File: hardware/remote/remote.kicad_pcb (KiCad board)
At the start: 2 copper layers, 106.7 x 86.4 mm, 27 parts

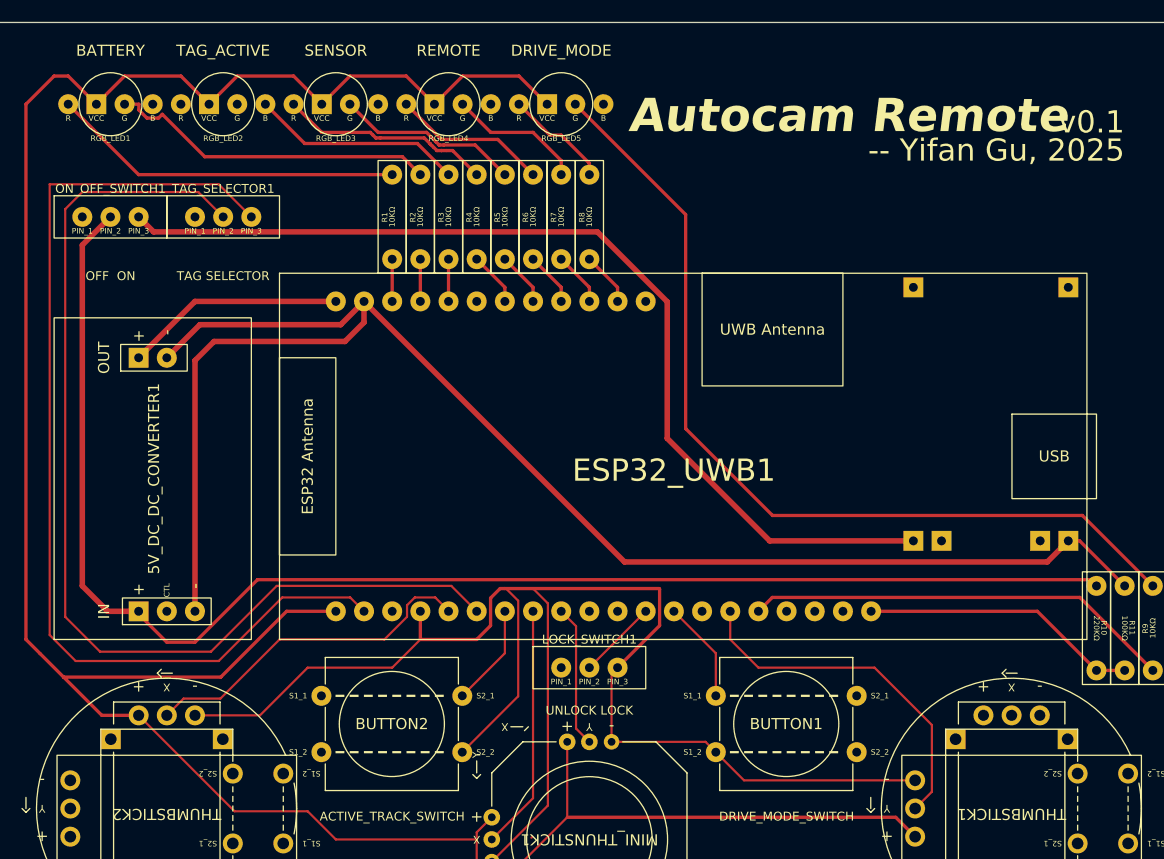
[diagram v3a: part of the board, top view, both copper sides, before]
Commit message: remote: Add UWB selector switch.
This switch will choose whether to use tag or the remote for the
distance measurement.

Also updated the PIN number and moved all non-uwb task to a separate
core.
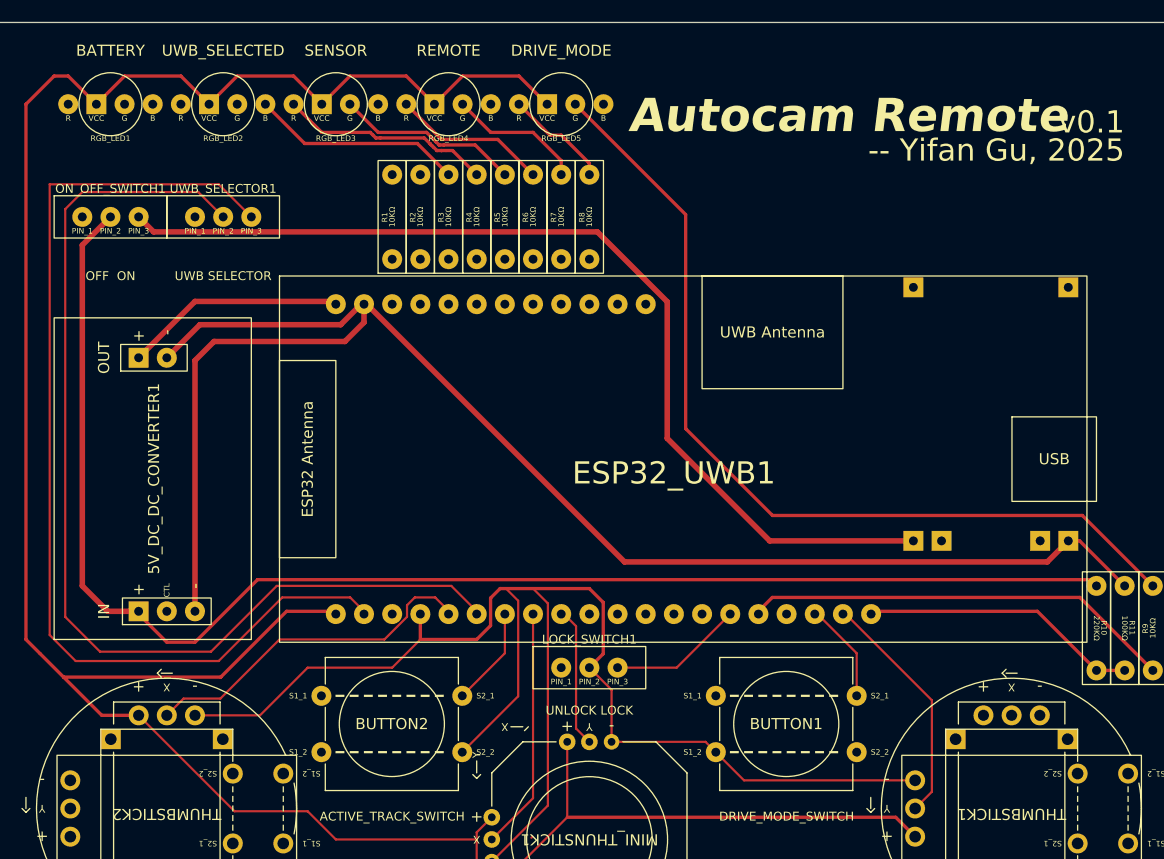
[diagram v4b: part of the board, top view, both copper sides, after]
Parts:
- RGB_LED2: value TAG_ACTIVE -> UWB_SELECTED
- UWB_SELECTOR1: renamed from TAG_SELECTOR1; value TAG SELECTOR -> UWB SELECTOR
- moved ESP32_UWB1 0.25 mm to (119.4, 83.8)
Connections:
- BUTTON1 pad 1: Net-(BUTTON1-S1_1) -> unconnected-(BUTTON1-S1_1-Pad1)
- BUTTON1 pad 3: unconnected-(BUTTON1-S2_1-Pad3) -> Net-(BUTTON1-S2_1)
- ESP32_UWB1 pad 12: Net-(ESP32_UWB1-IO25) -> unconnected-(ESP32_UWB1-IO25-Pad12)
- ESP32_UWB1 pad 13: Net-(BUTTON1-S1_1) -> unconnected-(ESP32_UWB1-IO26-Pad13)
- ESP32_UWB1 pad 18: unconnected-(ESP32_UWB1-IO35-Pad18) -> Net-(BUTTON1-S2_1)
- ESP32_UWB1 pad 19: unconnected-(ESP32_UWB1-IO36-Pad19) -> Net-(ESP32_UWB1-IO36)
- LOCK_SWITCH1 pad 2: Net-(ESP32_UWB1-IO25) -> Net-(BUTTON1-S1_2)
- LOCK_SWITCH1 pad 3: Net-(BUTTON1-S1_2) -> Net-(ESP32_UWB1-IO32)
- THUMBSTICK1 pad 5: Net-(ESP32_UWB1-IO32) -> Net-(ESP32_UWB1-IO36)
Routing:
- net Net-(RGB_LED1-R): track 31.8 -> 0.00 mm
- net Net-(RGB_LED1-G): track 29.9 -> 0.00 mm
- net Net-(ESP32_UWB1-IO36): track 0.00 -> 21.7 mm
- net Net-(ESP32_UWB1-IO32): track 32.1 -> 12.9 mm
- net Net-(BUTTON1-S2_1): track 0.00 -> 9.19 mm
- net Net-(BUTTON1-S1_1): track 9.19 -> 0.00 mm
- net Net-(ESP32_UWB1-IO25): track 7.18 -> 0.00 mm
- net Net-(BUTTON1-S1_2): track 139.7 -> 132.9 mm
- net Net-(ESP32_UWB1-IO22): track 4.86 -> 0.00 mm
- net Net-(ESP32_UWB1-IO16): track 4.86 -> 0.00 mm
- net Net-(ESP32_UWB1-IO5): track 4.86 -> 0.00 mm
- net Net-(ESP32_UWB1-IO21): track 4.86 -> 0.00 mm
- net Net-(ESP32_UWB1-IO17): track 4.86 -> 0.00 mm
- net Net-(ESP32_UWB1-IO3): track 3.81 -> 0.00 mm
- net Net-(ESP32_UWB1-IO1): track 3.81 -> 0.00 mm
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
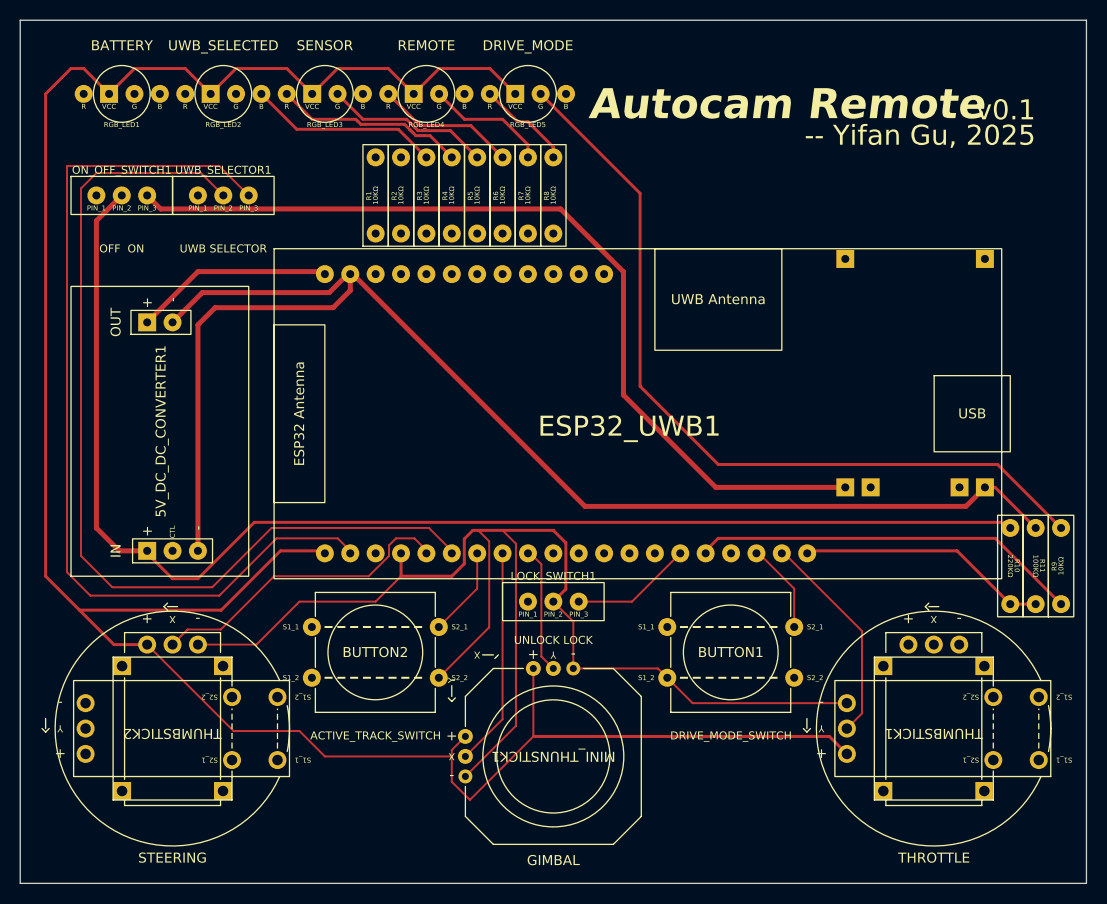
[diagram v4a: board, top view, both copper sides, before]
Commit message: hardware: Reroute the wires to fix unavailable PINs.
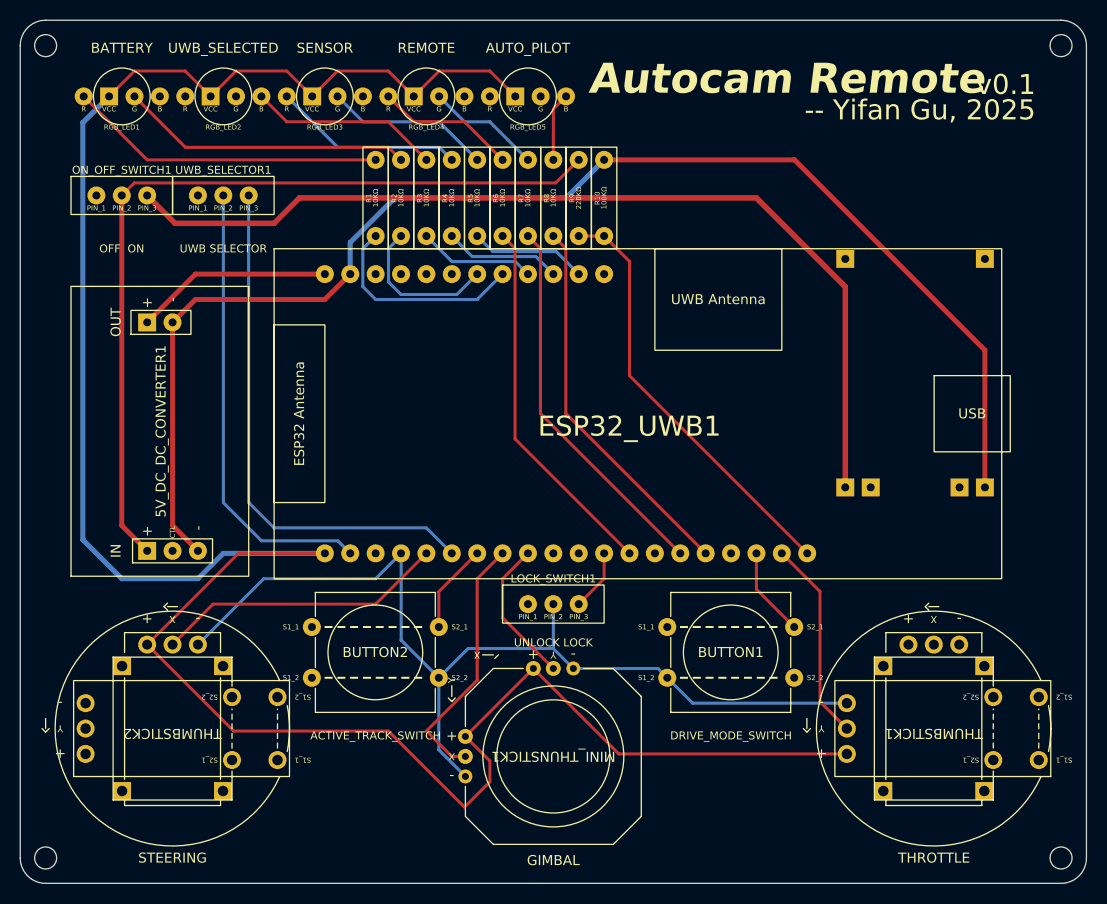
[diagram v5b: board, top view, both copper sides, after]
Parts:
- removed the R8 at (147.3, 82.3)
- added REF**: MountingHole_2.2mm_M2, MountingHole:MountingHole_2.2mm_M2, F.Cu at (198.1, 144.8)
- added REF**: MountingHole_2.2mm_M2, MountingHole:MountingHole_2.2mm_M2, F.Cu at (198.1, 63.5)
- added REF**: MountingHole_2.2mm_M2, MountingHole:MountingHole_2.2mm_M2, F.Cu at (96.5, 144.8)
- added REF**: MountingHole_2.2mm_M2, MountingHole:MountingHole_2.2mm_M2, F.Cu at (96.5, 63.5)
- RGB_LED5: value DRIVE_MODE -> AUTO_PILOT
- moved R8 62.7 mm to (147.3, 82.5)
- moved R10 52.1 mm to (152.4, 82.5), turned to 90 degrees
- moved R9 52.1 mm to (149.9, 82.5), turned to 90 degrees
- moved R6 2.55 mm to (142.2, 82.5)
- moved R7 2.55 mm to (144.8, 82.5)
- moved LOCK_SWITCH1 0.25 mm to (144.8, 119.4)
- moved R1 0.25 mm to (129.5, 82.5)
- moved R2 0.25 mm to (132.1, 82.5)
- moved R3 0.25 mm to (134.6, 82.5)
- moved R4 0.25 mm to (137.2, 82.5)
- moved R5 0.25 mm to (139.7, 82.5)
- moved RGB_LED1 0.25 mm to (104.1, 68.6)
- moved RGB_LED2 0.25 mm to (114.3, 68.6)
- moved RGB_LED3 0.25 mm to (124.5, 68.6)
- moved RGB_LED4 0.25 mm to (134.6, 68.6)
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- renumbered R11 to R10, R7 to R6, R6 to R7, R9 to R8, R10 to R9
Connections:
- ESP32_UWB1 pad 12: unconnected-(ESP32_UWB1-IO25-Pad12) -> Net-(ESP32_UWB1-IO25)
- ESP32_UWB1 pad 13: unconnected-(ESP32_UWB1-IO26-Pad13) -> Net-(ESP32_UWB1-IO26)
- ESP32_UWB1 pad 23: Net-(ESP32_UWB1-IO3) -> unconnected-(ESP32_UWB1-IO3-Pad23)
- ESP32_UWB1 pad 24: Net-(ESP32_UWB1-IO1) -> unconnected-(ESP32_UWB1-IO1-Pad24)
- ESP32_UWB1 pad 25: Net-(ESP32_UWB1-IO0) -> unconnected-(ESP32_UWB1-IO0-Pad25)
- LOCK_SWITCH1 pad 3: Net-(ESP32_UWB1-IO32) -> Net-(ESP32_UWB1-IO25)
- R1 pad 1: Net-(ESP32_UWB1-IO3) -> Net-(ESP32_UWB1-IO16)
- R10 pad 1: Net-(3.7V_BATTERY_CHARGER1-OUT-) -> Net-(ESP32_UWB1-IO39)
- R10 pad 2: Net-(ESP32_UWB1-IO39) -> Net-(3.7V_BATTERY_CHARGER1-OUT-)
- R2 pad 1: Net-(ESP32_UWB1-IO1) -> Net-(ESP32_UWB1-IO5)
- R3 pad 1: Net-(ESP32_UWB1-IO0) -> Net-(ESP32_UWB1-IO17)
- R4 pad 1: Net-(ESP32_UWB1-IO5) -> Net-(ESP32_UWB1-IO21)
- R5 pad 1: Net-(ESP32_UWB1-IO16) -> Net-(ESP32_UWB1-IO22)
- R6 pad 1: Net-(ESP32_UWB1-IO21) -> Net-(ESP32_UWB1-IO26)
- R6 pad 2: Net-(RGB_LED4-G) -> Net-(RGB_LED4-R)
- R7 pad 1: Net-(ESP32_UWB1-IO17) -> Net-(ESP32_UWB1-IO32)
- R7 pad 2: Net-(RGB_LED4-R) -> Net-(RGB_LED4-G)
- R8 pad 2: Net-(RGB_LED5-G) -> Net-(RGB_LED5-B)
- R9 pad 1: Net-(5V_DC_DC_CONVERTER1-IN_+) -> Net-(ESP32_UWB1-IO39)
- R9 pad 2: Net-(ESP32_UWB1-IO39) -> Net-(5V_DC_DC_CONVERTER1-IN_+)
- RGB_LED5 pad 1: Net-(RGB_LED5-R) -> unconnected-(RGB_LED5-R-Pad1)
- RGB_LED5 pad 3: Net-(RGB_LED5-G) -> unconnected-(RGB_LED5-G-Pad3)
- RGB_LED5 pad 4: unconnected-(RGB_LED5-B-Pad4) -> Net-(RGB_LED5-B)
- UWB_SELECTOR1 pad 2: Net-(ESP32_UWB1-IO12) -> Net-(ESP32_UWB1-GND-Pad2)
- UWB_SELECTOR1 pad 3: Net-(ESP32_UWB1-GND-Pad2) -> Net-(ESP32_UWB1-IO12)
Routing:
- net Net-(RGB_LED5-G): track 81.4 -> 0.00 mm
- net Net-(ESP32_UWB1-GND-Pad2): track 92.2 -> 45.5 mm
- net Net-(5V_DC_DC_CONVERTER1-IN_+): track 129.8 -> 83.8 mm
- net Net-(ESP32_UWB1-IO12): track 94.4 -> 53.2 mm
- net Net-(ESP32_UWB1-IO26): track 0.00 -> 37.0 mm
- net Net-(BUTTON1-S1_2): track 132.9 -> 97.8 mm
- net Net-(RGB_LED1-R): track 0.00 -> 31.8 mm
- net Net-(RGB_LED1-G): track 0.00 -> 29.3 mm
- net Net-(ESP32_UWB1-IO32): track 12.9 -> 38.1 mm
- net Net-(ESP32_UWB1-IO16): track 0.00 -> 21.2 mm
- net Net-(ESP32_UWB1-IO39): track 25.1 -> 42.7 mm
- net Net-(ESP32_UWB1-IO5): track 0.00 -> 15.3 mm
- net Net-(ESP32_UWB1-IO22): track 0.00 -> 11.7 mm
- net Net-(ESP32_UWB1-IO21): track 0.00 -> 11.7 mm
- net Net-(ESP32_UWB1-IO17): track 0.00 -> 11.7 mm
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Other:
- outline, holes or cut-outs redrawn
